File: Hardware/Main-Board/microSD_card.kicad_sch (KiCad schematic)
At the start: 4 parts

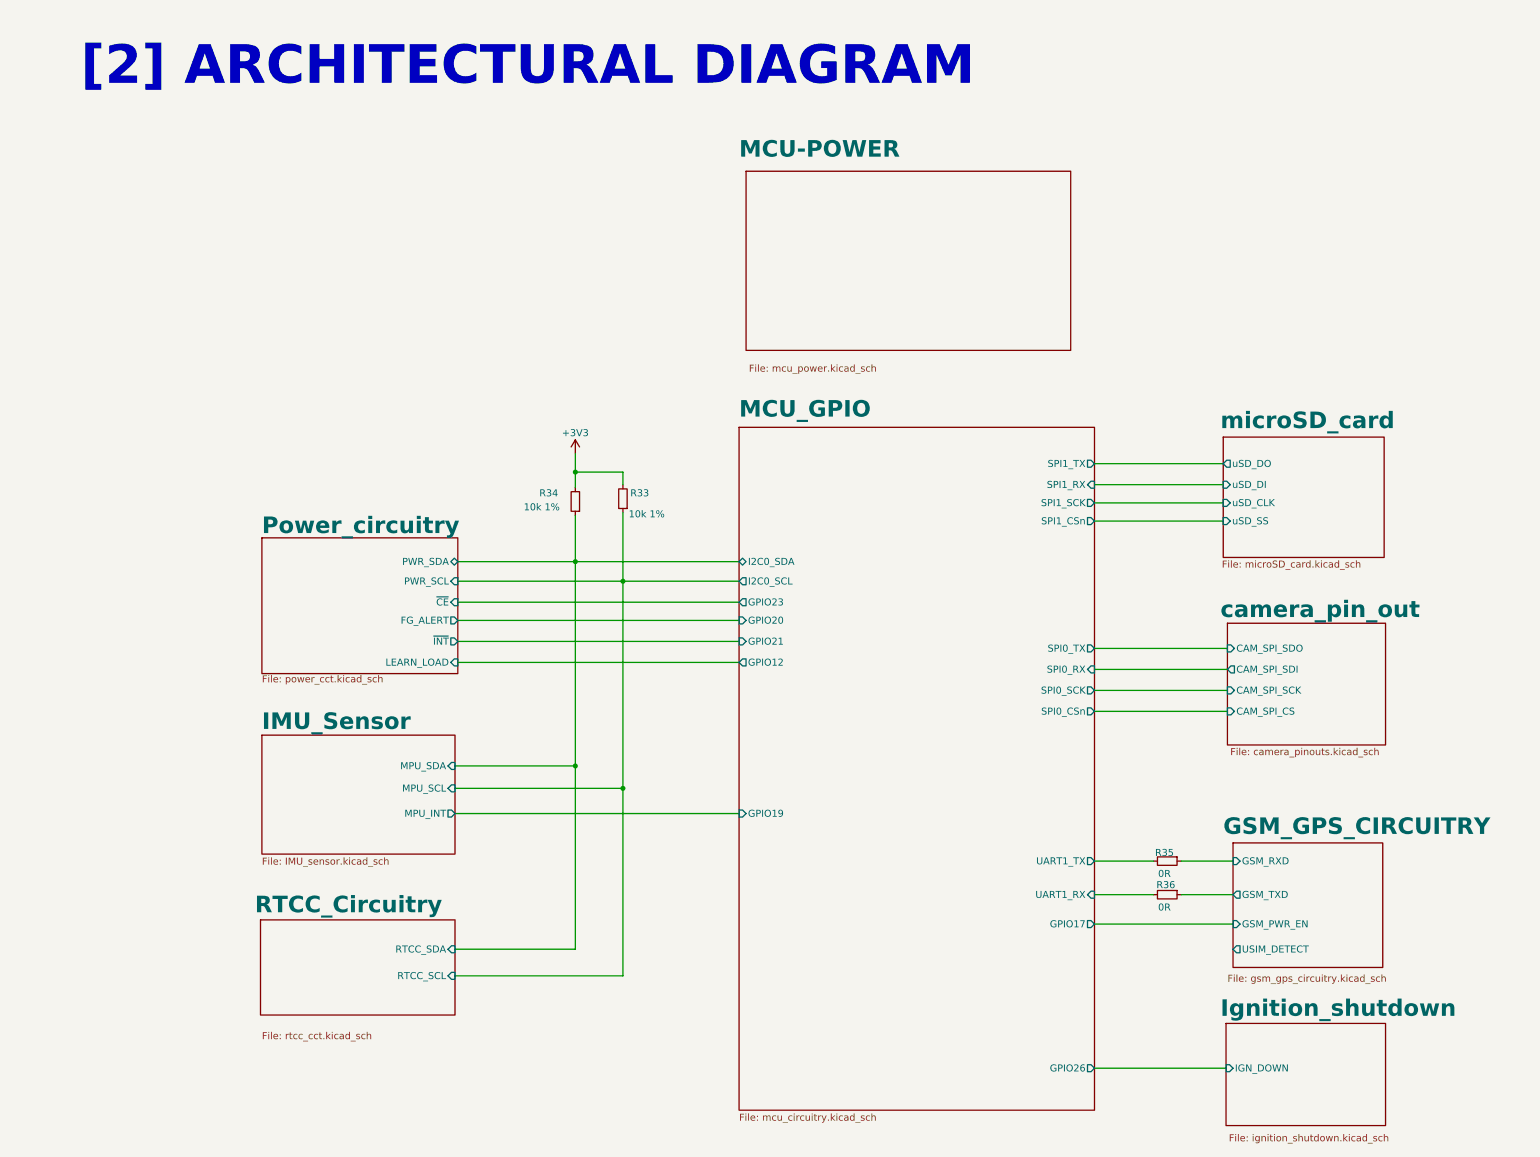
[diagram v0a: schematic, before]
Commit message: Done with main board design, and camera interconnect in progress
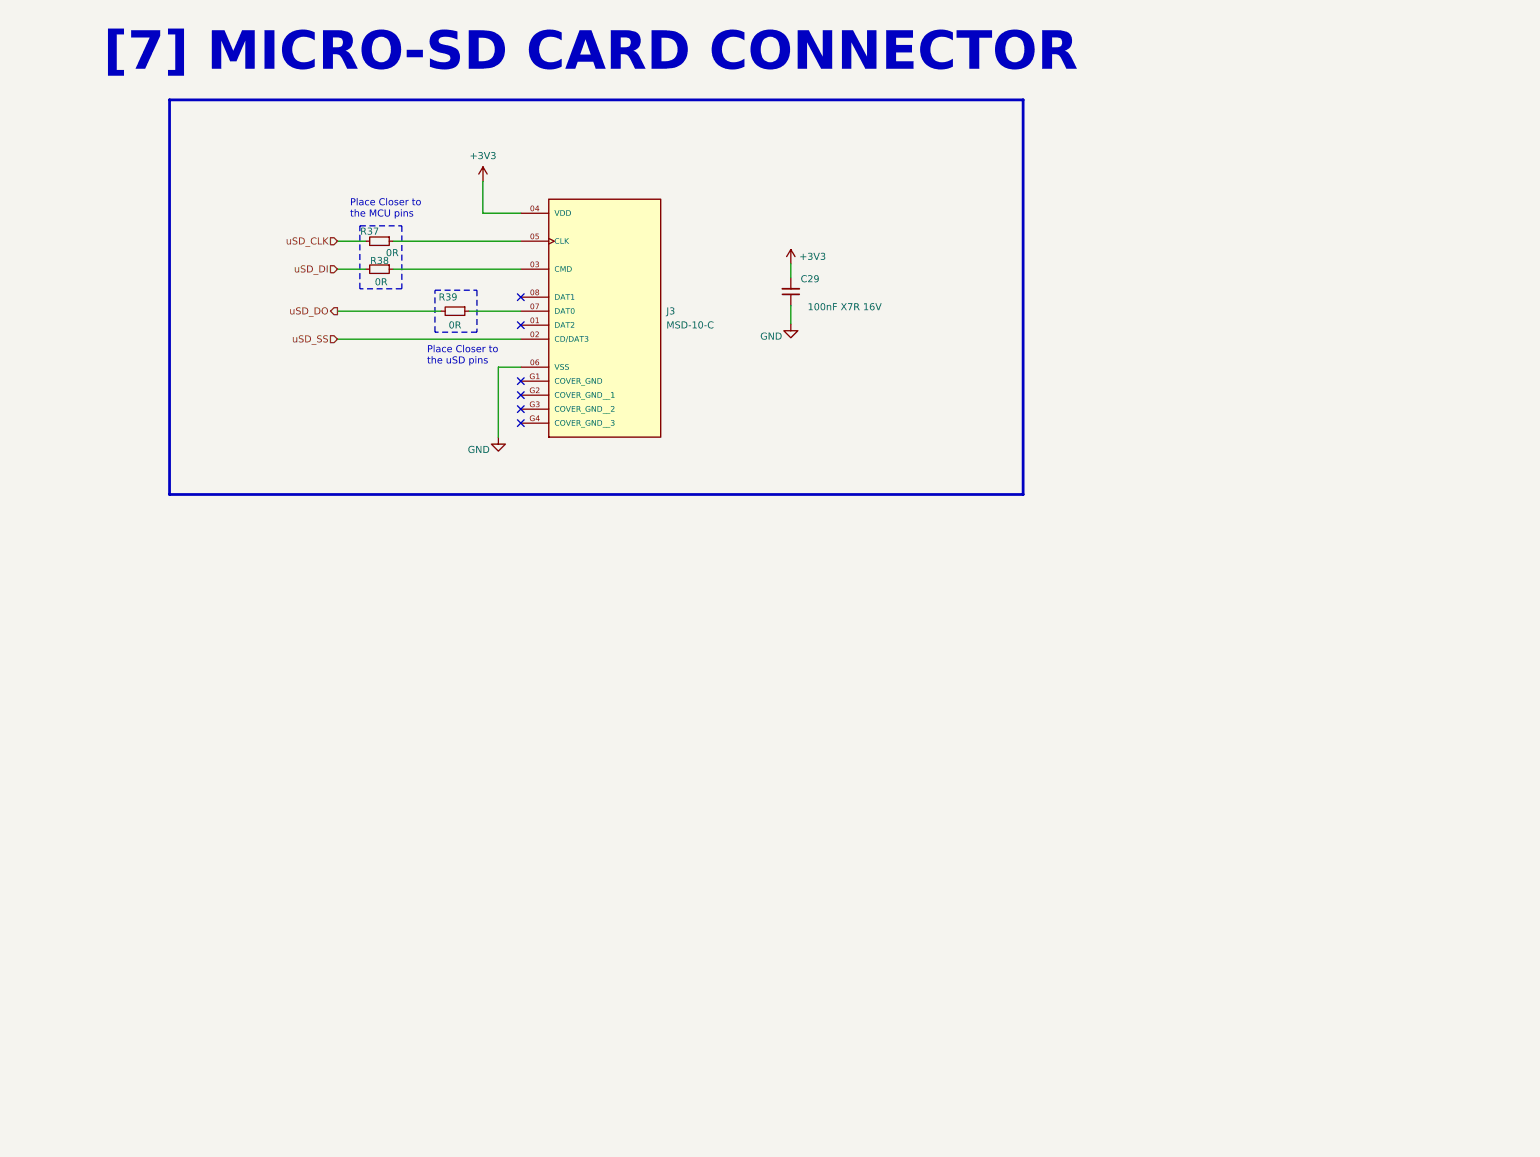
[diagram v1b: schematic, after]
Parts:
- removed R33, R34: 10k 1%, Resistor_SMD:R_0402_1005Metric, symbol Device:R_Small
- removed R35, R36: 0R, Resistor_SMD:R_0402_1005Metric, symbol Device:R_Small
- added C29: 100nF X7R 16V, Capacitor_SMD:C_0402_1005Metric, symbol Device:C_Small
- added J3: MSD-10-C, MSD_10_C:CUI_MSD-10-C, symbol MSD-10-C:MSD-10-C
- added R37, R38, R39: 0R, Resistor_SMD:R_0402_1005Metric, symbol Device:R_Small
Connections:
- net +3V3: now also C29.2, J3.04 (VDD)
- new net: J3.03 (CMD), R38.1
- new net: J3.05 (CLK), R37.1
- new net: J3.07 (DAT0), R39.1
- new net GND: C29.1, J3.06 (VSS)
- new net uSD_CLK: R37.2
- new net uSD_DI: R38.2
- new net uSD_DO: R39.2
- new net uSD_SS: J3.02 (CD/DAT3)
- no-connect marks 0 -> 6
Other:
- removed sheet GSM_GPS_CIRCUITRY
- removed sheet IMU_Sensor
- removed sheet Ignition_shutdown
- removed sheet MCU-POWER
- removed sheet MCU_GPIO
- removed sheet Power_circuitry
- removed sheet RTCC_Circuitry
- removed sheet camera_pin_out
- removed sheet microSD_card
- note added: "Place Closer to the MCU pins"
- note added: "Place Closer to the uSD pins"
- note added: "[7] MICRO-SD CARD CONNECTOR"
- note removed: "[2] ARCHITECTURAL DIAGRAM"
